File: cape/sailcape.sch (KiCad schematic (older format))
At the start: 1 part

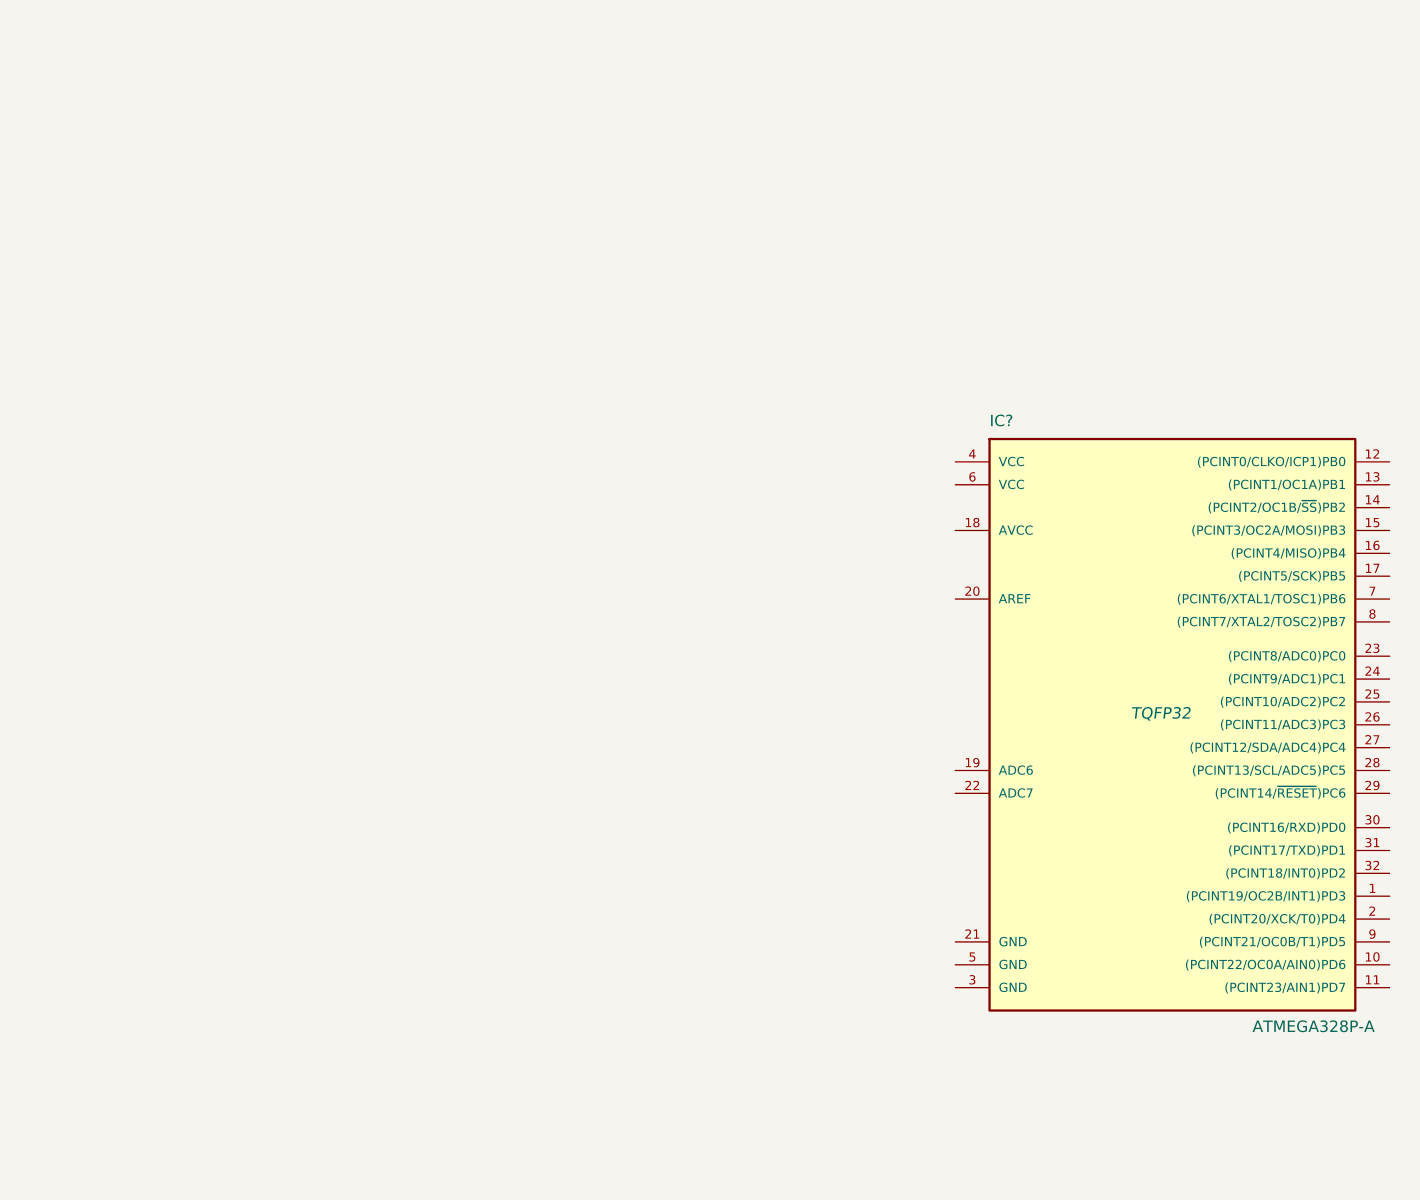
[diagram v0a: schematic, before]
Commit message: wired up in system programming and graphical wingsail can now construct
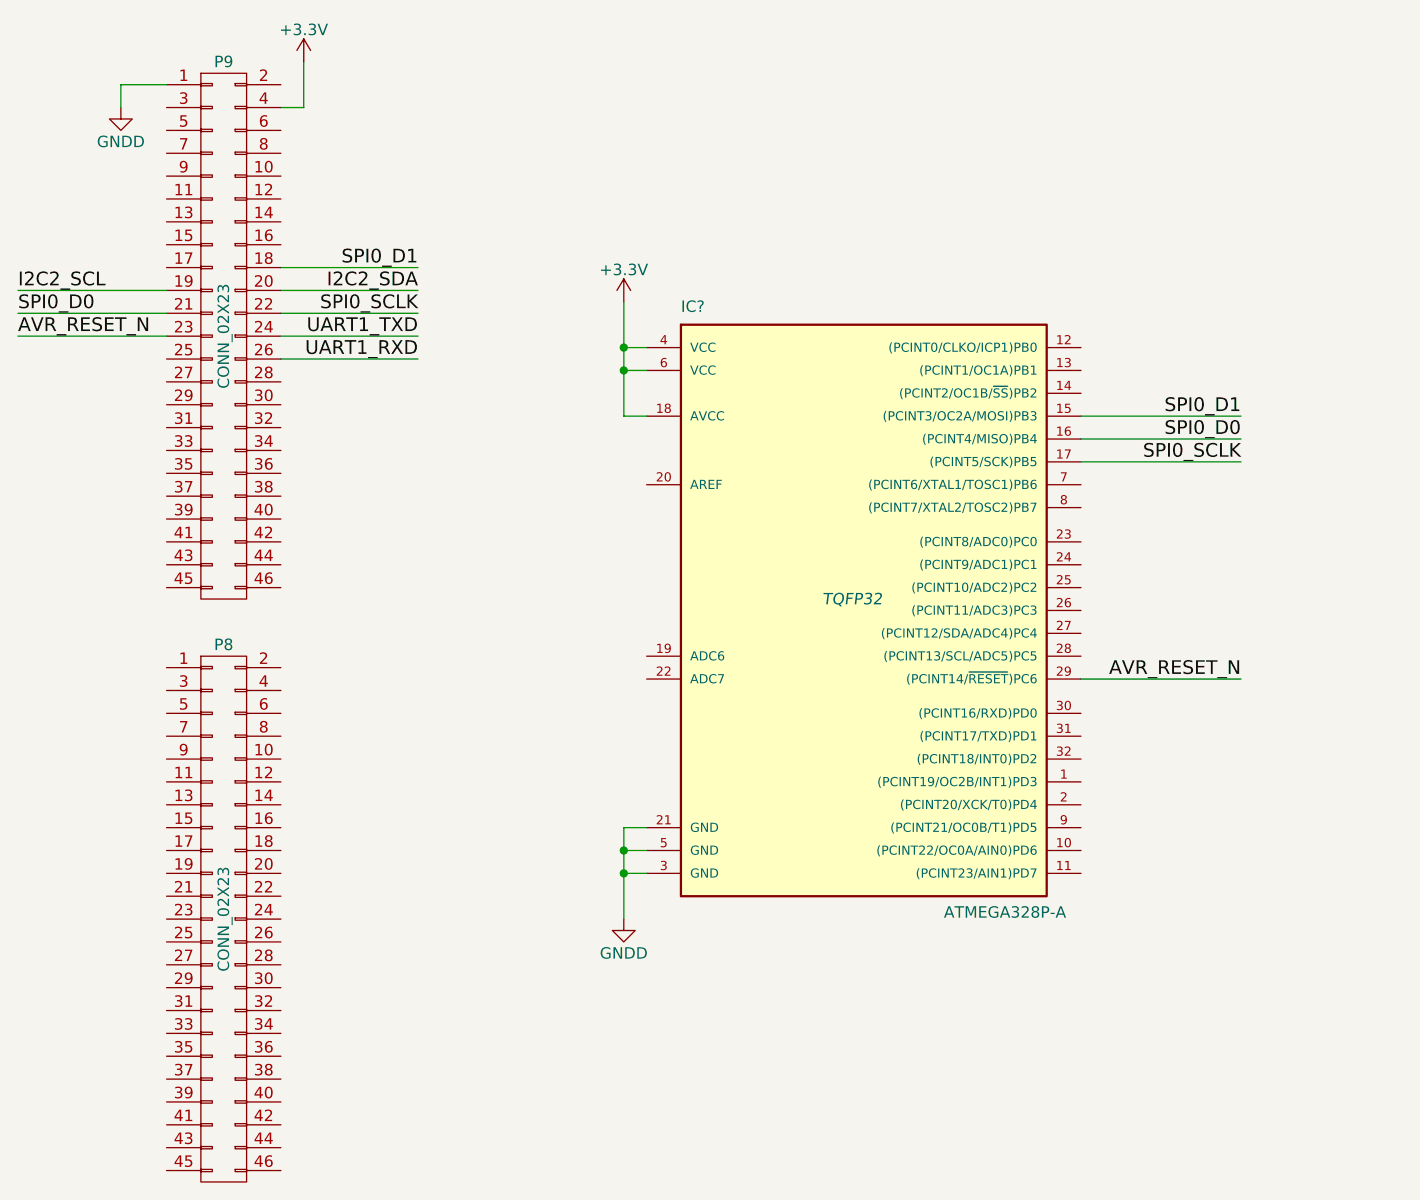
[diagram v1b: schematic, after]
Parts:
- added P8, P9: CONN_02X23, symbol CONN_02X23
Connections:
- net SPI0_D1: now reaches IC?.15 ((PCINT3/OC2A/MOSI)PB3)
- net SPI0_D1: now also P9.18 (P18)
- net SPI0_D0: now reaches IC?.16 ((PCINT4/MISO)PB4)
- net SPI0_D0: now also P9.21 (P21)
- net SPI0_SCLK: now reaches IC?.17 ((PCINT5/SCK)PB5)
- net SPI0_SCLK: now also P9.22 (P22)
- net +3V3: now reaches IC?.18 (AVCC)
- net +3V3: now also IC?.4 (VCC), IC?.6 (VCC), P9.4 (P4)
- net GNDD: now reaches IC?.21 (GND)
- net GNDD: now also IC?.3 (GND), IC?.5 (GND), P9.1 (P1)
- net AVR_RESET_N: now reaches IC?.29 ((PCINT14/~RESET~)PC6)
- net AVR_RESET_N: now also P9.23 (P23)
- new net I2C2_SCL: P9.19 (P19)
- new net I2C2_SDA: P9.20 (P20)
- new net UART1_RXD: P9.26 (P26)
- new net UART1_TXD: P9.24 (P24)
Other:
- moved on the sheet: IC?
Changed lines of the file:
@@
 LIBS:contrib
 LIBS:valves
+LIBS:sailcape-cache
 EELAYER 25 0
 EELAYER END
@@
 L ATMEGA328P-A IC?
 U 1 1 597B5A3F
-P 5600 3550
-F 0 "IC?" H 4850 4800 50  0000 L BNN
-F 1 "ATMEGA328P-A" H 6000 2150 50  0000 L BNN
-F 2 "TQFP32" H 5600 3550 50  0000 C CIN
-F 3 "" H 5600 3550 50  0000 C CNN
-	1    5600 3550
+P 4250 3050
+F 0 "IC?" H 3500 4300 50  0000 L BNN
+F 1 "ATMEGA328P-A" H 4650 1650 50  0000 L BNN
+F 2 "TQFP32" H 4250 3050 50  0000 C CIN
+F 3 "" H 4250 3050 50  0000 C CNN
+	1    4250 3050
 	1    0    0    -1
 $EndComp
+$Comp
+L CONN_02X23 P8
+U 1 1 597BA15D
+P 1500 4450
+F 0 "P8" H 1500 5650 50  0000 C CNN
+F 1 "CONN_02X23" V 1500 4450 50  0000 C CNN
+F 2 "" H 1500 3600 50  0000 C CNN
+F 3 "" H 1500 3600 50  0000 C CNN
+	1    1500 4450
+	1    0    0    -1
+$EndComp
+$Comp
+L CONN_02X23 P9
+U 1 1 597BA24C
+P 1500 1900
+F 0 "P9" H 1500 3100 50  0000 C CNN
+F 1 "CONN_02X23" V 1500 1900 50  0000 C CNN
+F 2 "" H 1500 1050 50  0000 C CNN
+F 3 "" H 1500 1050 50  0000 C CNN
+	1    1500 1900
+	1    0    0    -1
+$EndComp
+$Comp
+L GNDD #PWR?
+U 1 1 597BA958
+P 1050 900
+F 0 "#PWR?" H 1050 650 50  0001 C CNN
+F 1 "GNDD" H 1050 750 50  0000 C CNN
+F 2 "" H 1050 900 50  0000 C CNN
+F 3 "" H 1050 900 50  0000 C CNN
+	1    1050 900
+	1    0    0    -1
+$EndComp
+$Comp
+L +3.3V #PWR?
+U 1 1 597BA972
+P 1850 700
+F 0 "#PWR?" H 1850 550 50  0001 C CNN
+F 1 "+3.3V" H 1850 840 50  0000 C CNN
+F 2 "" H 1850 700 50  0000 C CNN
+F 3 "" H 1850 700 50  0000 C CNN
+	1    1850 700
+	1    0    0    -1
+$EndComp
+Text Label 2350 1700 2    60   ~ 0
+I2C2_SDA
+Text Label 2350 1800 2    60   ~ 0
+SPI0_SCLK
+Text Label 2350 1900 2    60   ~ 0
+UART1_TXD
+Text Label 2350 2000 2    60   ~ 0
+UART1_RXD
+Text Label 2350 1600 2    60   ~ 0
+SPI0_D1
+Text Label 600  1800 0    60   ~ 0
+SPI0_D0
+Text Label 600  1700 0    60   ~ 0
+I2C2_SCL
+Text Label 600  1900 0    60   ~ 0
+AVR_RESET_N
+$Comp
+L +3.3V #PWR?
+U 1 1 597BB49D
+P 3250 1750
+F 0 "#PWR?" H 3250 1600 50  0001 C CNN
+F 1 "+3.3V" H 3250 1890 50  0000 C CNN
+F 2 "" H 3250 1750 50  0000 C CNN
+F 3 "" H 3250 1750 50  0000 C CNN
+	1    3250 1750
+	1    0    0    -1
+$EndComp
+Wire Wire Line
+	1050 900  1050 800
+Wire Wire Line
+	1050 800  1250 800
+Wire Wire Line
+	1850 700  1850 900
+Wire Wire Line
+	1850 900  1750 900
+Wire Wire Line
+	1750 1600 2350 1600
+Wire Wire Line
+	1750 1700 2350 1700
+Wire Wire Line
+	1750 1800 2350 1800
+Wire Wire Line
+	1750 1900 2350 1900
+Wire Wire Line
+	1750 2000 2350 2000
+Wire Wire Line
+	1250 1700 600  1700
+Wire Wire Line
+	1250 1800 600  1800
+Wire Wire Line
+	1250 1900 600  1900
+$Comp
+L GNDD #PWR?
+U 1 1 597BB571
+P 3250 4450
+F 0 "#PWR?" H 3250 4200 50  0001 C CNN
+F 1 "GNDD" H 3250 4300 50  0000 C CNN
+F 2 "" H 3250 4450 50  0000 C CNN
+F 3 "" H 3250 4450 50  0000 C CNN
+	1    3250 4450
+	1    0    0    -1
+$EndComp
+Wire Wire Line
+	3350 4050 3250 4050
+Wire Wire Line
+	3250 4050 3250 4450
+Wire Wire Line
+	3350 4150 3250 4150
+Connection ~ 3250 4150
+Wire Wire Line
+	3350 4250 3250 4250
+Connection ~ 3250 4250
+Wire Wire Line
+	3350 2050 3250 2050
+Wire Wire Line
+	3250 1750 3250 2250
+Wire Wire Line
+	3350 1950 3250 1950
+Connection ~ 3250 1950
+Text Label 5950 2250 2    60   ~ 0
+SPI0_D1
+Text Label 5950 2450 2    60   ~ 0
+SPI0_SCLK
+Text Label 5950 2350 2    60   ~ 0
+SPI0_D0
+Text Label 5950 3400 2    60   ~ 0
+AVR_RESET_N
+Wire Wire Line
+	5250 2250 5950 2250
+Wire Wire Line
+	5250 2350 5950 2350
+Wire Wire Line
+	5250 2450 5950 2450
+Wire Wire Line
+	5250 3400 5950 3400
+Wire Wire Line
+	3250 2250 3350 2250
+Connection ~ 3250 2050
 $EndSCHEMATC
